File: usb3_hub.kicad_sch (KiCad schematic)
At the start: 62 parts, among them Q2601 QS6M4, U2601 UPD720210K8-BAF-A, Y2601 24MHz

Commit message: Reannotate the board
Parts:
- added C89: 1uF, Capacitor_SMD:C_0402_1005Metric, symbol Device:C_Small
- added C90, C91: 4.7uF, Capacitor_SMD:C_0603_1608Metric, symbol Device:C_Small
- added R88: 15k, Resistor_SMD:R_0402_1005Metric, symbol Device:R_Small
- renumbered C2614 to C100, C2615 to C101, C2616 to C102, C2617 to C103, C2618 to C104, C2619 to C105, C2620 to C106, C2621 to C107, C2622 to C108, C2623 to C109, C2624 to C110, C2625 to C111, C2626 to C112, C2627 to C113, C2628 to C114, C2629 to C115, C2630 to C116, C2631 to C117, C2632 to C118, C2633 to C119, C2634 to C120, C2601 to C84, C2602 to C85, C2603 to C86, C2604 to C87, C2605 to C88, C2606 to C92, C2607 to C93, C2608 to C94, C2609 to C95, C2610 to C96, C2611 to C97, C2612 to C98, C2613 to C99, D2601 to D23, FB2601 to FB2, L2601 to L5, NT2601 to NT1, Q2601 to Q7, R2601 to R68, R2602 to R69, R2603 to R70, R2604 to R71, R2605 to R72, R2606 to R73, R2607 to R74, R2608 to R75, R2609 to R76, R2610 to R77, R2611 to R78, R2612 to R79, R2613 to R80, R2614 to R81, R2615 to R82, R2616 to R83, R2617 to R84, R2618 to R85, R2619 to R86, R2620 to R87, TP2601 to TP29, U2601 to U33, Y2601 to Y2
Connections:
- net +5V: now also U33.49 (V50IN), C89.2, C90.1
- net GND: now also C89.1, C90.2, C91.2, R88.2; no longer U33.49 (V50IN)
- net V33OUT: now reaches U33.48 (V33OUT)
- net V33OUT: now also C91.1, R88.1
- no-connect marks 8 -> 7

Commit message: Add GND/3.3V/5V headers, add missing JLC part numbers
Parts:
- added TP36: TestPoint, TestPoint:TestPoint_Pad_D1.0mm, symbol Connector:TestPoint
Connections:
- net EN: now also TP36.1
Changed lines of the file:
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@@
 	)
 	(junction
+		(at 97.79 50.8)
+		(diameter 0)
+		(color 0 0 0 0)
+	)
+	(junction
 		(at 238.76 44.45)
 		(diameter 0)
@@
 	(wire
 		(pts
+			(xy 97.79 50.8) (xy 104.14 50.8)
+		)
+		(stroke
+			(width 0)
+			(type default)
+		)
+	)
+	(wire
+		(pts
 			(xy 208.28 143.51) (xy 210.82 143.51)
 		)
@@
 	(wire
 		(pts
-			(xy 102.87 50.8) (xy 104.14 50.8)
+			(xy 95.25 50.8) (xy 97.79 50.8)
 		)
 		(stroke
@@
 	(hierarchical_label "EN"
 		(shape input)
-		(at 102.87 50.8 180)
+		(at 95.25 50.8 180)
 		(effects
 			(font
@@
 					(unit 1)
 				)
+			)
+		)
+	)
+	(symbol
+		(lib_id "Connector:TestPoint")
+		(at 97.79 50.8 0)
+		(mirror y)
+		(unit 1)
+		(exclude_from_sim no)
+		(in_bom yes)
+		(on_board yes)
+		(dnp no)
+		(property "Reference" "TP36"
+			(at 102.87 43.434 90)
+			(effects
+				(font
+					(size 1.27 1.27)
+				)
+			)
+		)
+		(property "Value" "TestPoint"
+			(at 100.33 43.434 90)
+			(effects
+				(font
+					(size 1.27 1.27)
+				)
+			)
+		)
+		(property "Footprint" "TestPoint:TestPoint_Pad_D1.0mm"
+			(at 92.71 50.8 0)
+			(effects
+				(font
+					(size 1.27 1.27)
+				)
+				(hide yes)
+			)
+		)
+		(property "Datasheet" "~"
+			(at 92.71 50.8 0)
+			(effects
+				(font
+					(size 1.27 1.27)
+				)
+				(hide yes)
+			)
+		)
+		(property "Description" "test point"
+			(at 97.79 50.8 0)
+			(effects
+				(font
+					(size 1.27 1.27)
+				)
+				(hide yes)
+			)
+		)
+		(property "Characteristics" ""
+			(at 97.79 50.8 0)
+			(effects
+				(font
+					(size 1.27 1.27)
+				)
+				(hide yes)
+			)
+		)
+		(property "LCSC Part" ""
+			(at 97.79 50.8 0)
+			(effects
+				(font
+					(size 1.27 1.27)
+				)
+			)
+		)
+		(property "Field8" ""
+			(at 97.79 50.8 0)
+			(effects
+				(font
+					(size 1.27 1.27)
+				)
+			)
+		)
+		(property "PartNumber" ""
+			(at 97.79 50.8 0)
+			(effects
+				(font
+					(size 1.27 1.27)
+				)
+			)
+		)
+		(pin "1"
+		)
+		(instances
+			(project "HALPI2"
+				(path "/abc482bd-3f17-4d35-80db-1da3dcdb5c27/b774f543-305e-4249-92c3-c3de7e8a285e/306b39c2-3d43-4872-bf23-cfec09993877"
+					(reference "TP36")
+					(unit 1)
+				)

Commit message: FInal v0.2.0 proto changes
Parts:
- D23: JLCPCB_CORRECTION (none) -> 0;0;180
- Q7, R85: Component Class (none) -> fine_pitch
- renumbered C98 to C100, C99 to C101, C100 to C102, C101 to C103, C102 to C104, C103 to C105, C104 to C106, C105 to C107, C106 to C108, C107 to C109, C108 to C110, C109 to C111, C110 to C112, C111 to C113, C112 to C114, C113 to C115, C114 to C116, C115 to C117, C116 to C118, C117 to C119, C118 to C120, C119 to C121, C120 to C122, C84 to C86, C85 to C87, C86 to C88, C87 to C89, C88 to C90, C89 to C91, C90 to C92, C91 to C93, C92 to C94, C93 to C95, C94 to C96, C95 to C97, C96 to C98, C97 to C99, FB2 to FB4, TP36 to TP42, TP29 to TP43

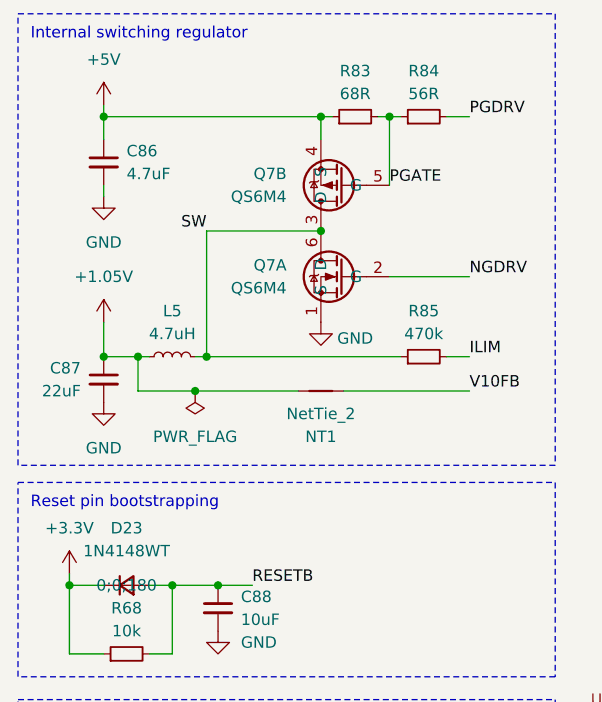
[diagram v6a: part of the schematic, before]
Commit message: Nailed the current limiter design
Also added more GND test pads
Also fixed the MCU I2C pinout
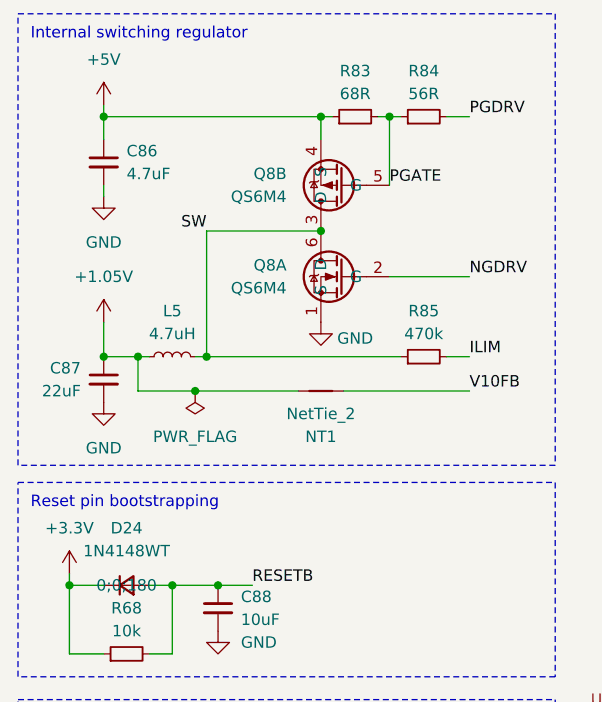
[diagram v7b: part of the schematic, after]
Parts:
- renumbered D23 to D24, Q7 to Q8
